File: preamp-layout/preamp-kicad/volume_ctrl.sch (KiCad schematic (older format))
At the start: 82 parts, among them J64 Conn_01x02_Male, J65 Conn_01x02_Male, J66 Conn_01x02_Male, J67 Conn_01x03_Female, J68 Conn_01x03_Female, J69 Conn_01x03_Male, J70 Conn_01x03_Male, J71 Conn_01x03_Male, U11 TL074CDR, U13 THAT2181, U14 THAT2181, U15 NJM2068M, U16 THAT2181, U17 THAT2181, U18 NJM2068M, U9 DAC5574

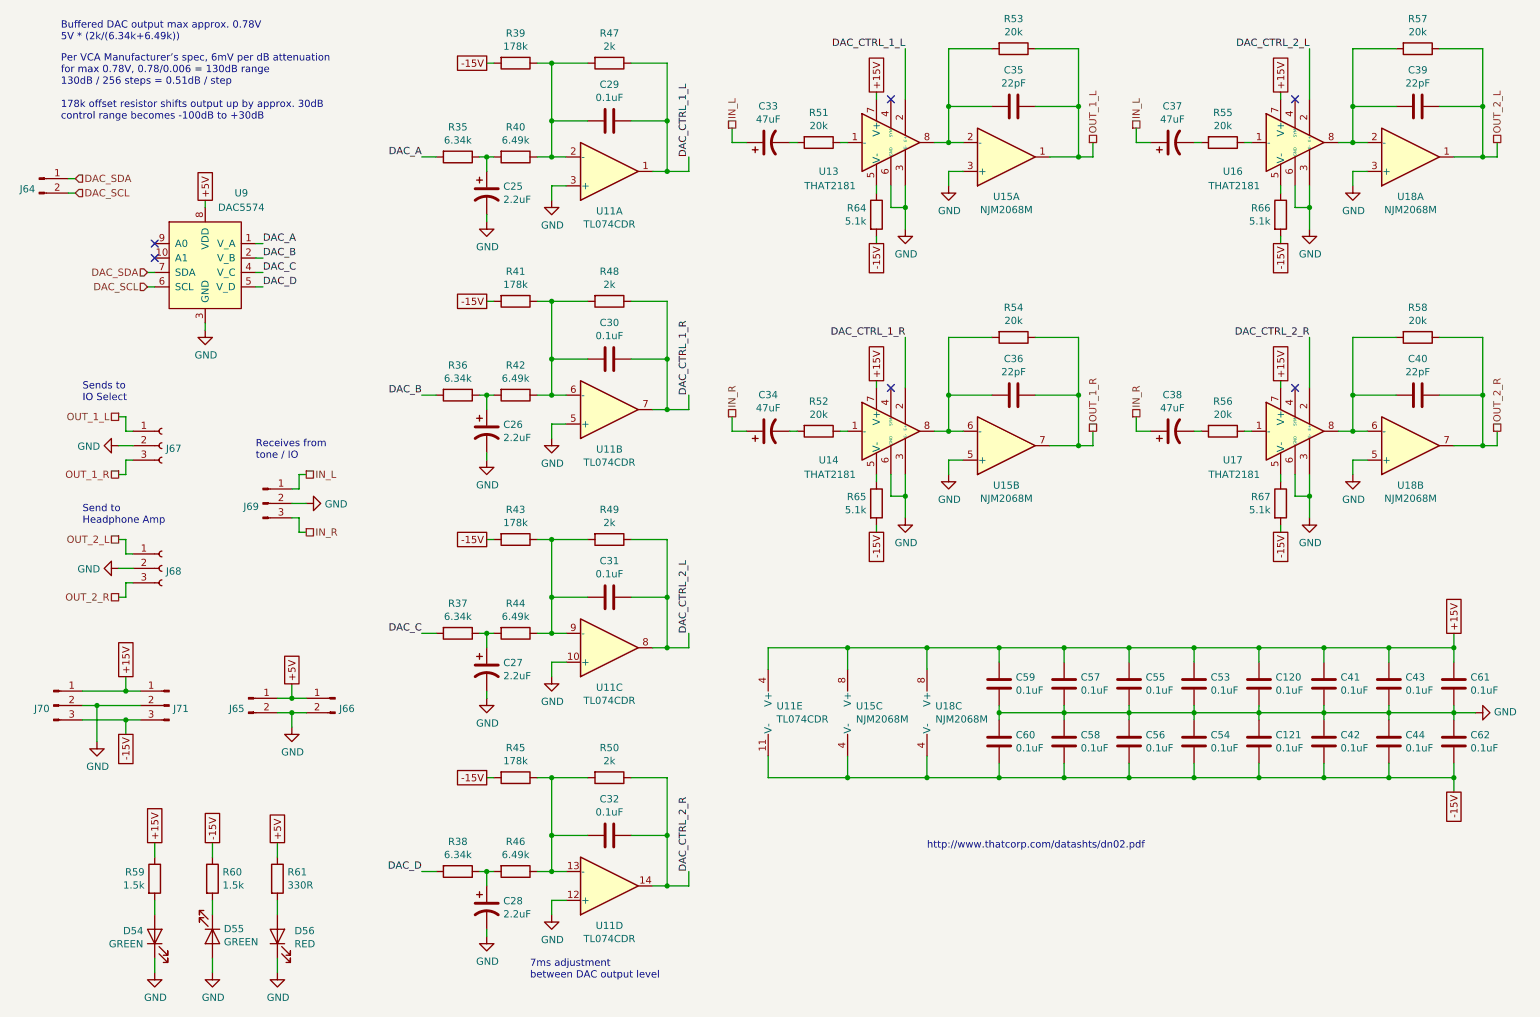
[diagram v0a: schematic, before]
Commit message: RefDes Update
Re-ran refdes assignment, updated BOM accordingly.
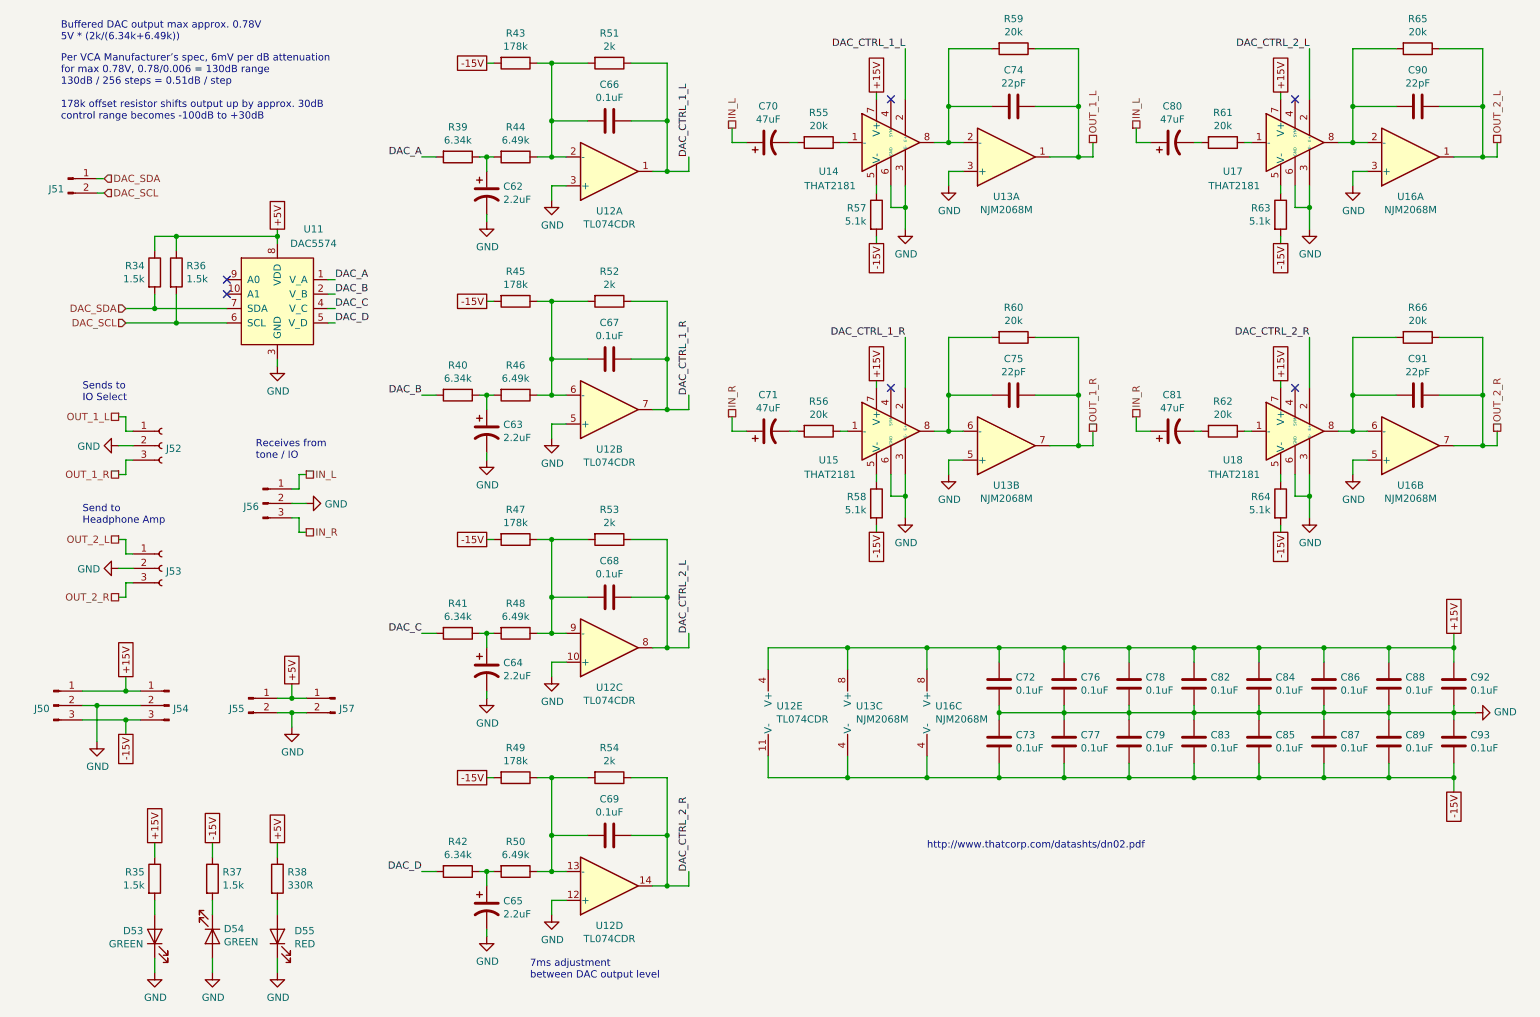
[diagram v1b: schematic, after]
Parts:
- added R34, R36: 1.5k, Resistor_SMD:R_1206_3216Metric_Pad1.42x1.75mm_HandSolder, symbol Device:R
- renumbered C25 to C62, C26 to C63, C27 to C64, C28 to C65, C29 to C66, C30 to C67, C31 to C68, C32 to C69, C33 to C70, C34 to C71, C59 to C72, C60 to C73, C35 to C74, C36 to C75, C57 to C76, C58 to C77, C55 to C78, C56 to C79, C37 to C80, C38 to C81, C53 to C82, C54 to C83, C120 to C84, C121 to C85, C41 to C86, C42 to C87, C43 to C88, C44 to C89, C39 to C90, C40 to C91, C61 to C92, C62 to C93, D54 to D53, D55 to D54, D56 to D55, J70 to J50, J64 to J51, J67 to J52, J68 to J53, J71 to J54, J65 to J55, J69 to J56, J66 to J57, R59 to R35, R60 to R37, R61 to R38, R35 to R39, R36 to R40, R37 to R41, R38 to R42, R39 to R43, R40 to R44, R41 to R45, R42 to R46, R43 to R47, R44 to R48, R45 to R49, R46 to R50, R47 to R51, R48 to R52, R49 to R53, R50 to R54, R51 to R55, R52 to R56, R64 to R57, R65 to R58, R53 to R59, R54 to R60, R55 to R61, R56 to R62, R66 to R63, R67 to R64, R57 to R65, R58 to R66, U9 to U11, U11 to U12, U15 to U13, U13 to U14, U14 to U15, U18 to U16, U16 to U17, U17 to U18
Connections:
- net +5V: now also R34.1, R36.1
- net DAC_SCL: now also R36.2
- net DAC_SDA: now also R34.2
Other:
- moved on the sheet: J51, U11

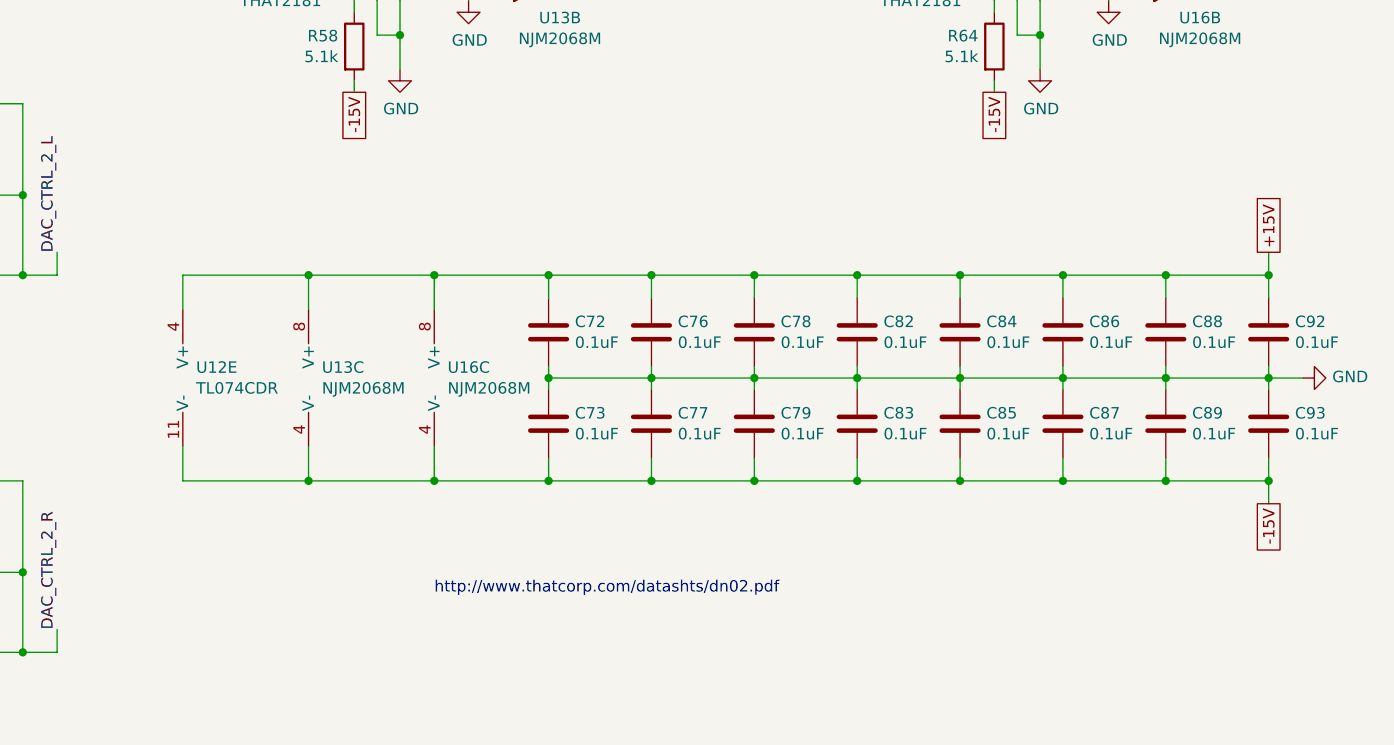
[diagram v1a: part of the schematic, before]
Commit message: Prelim PCB layout
Work done to lay out PCBs. Saving in anticipation of creating branch with a different input switching topology.
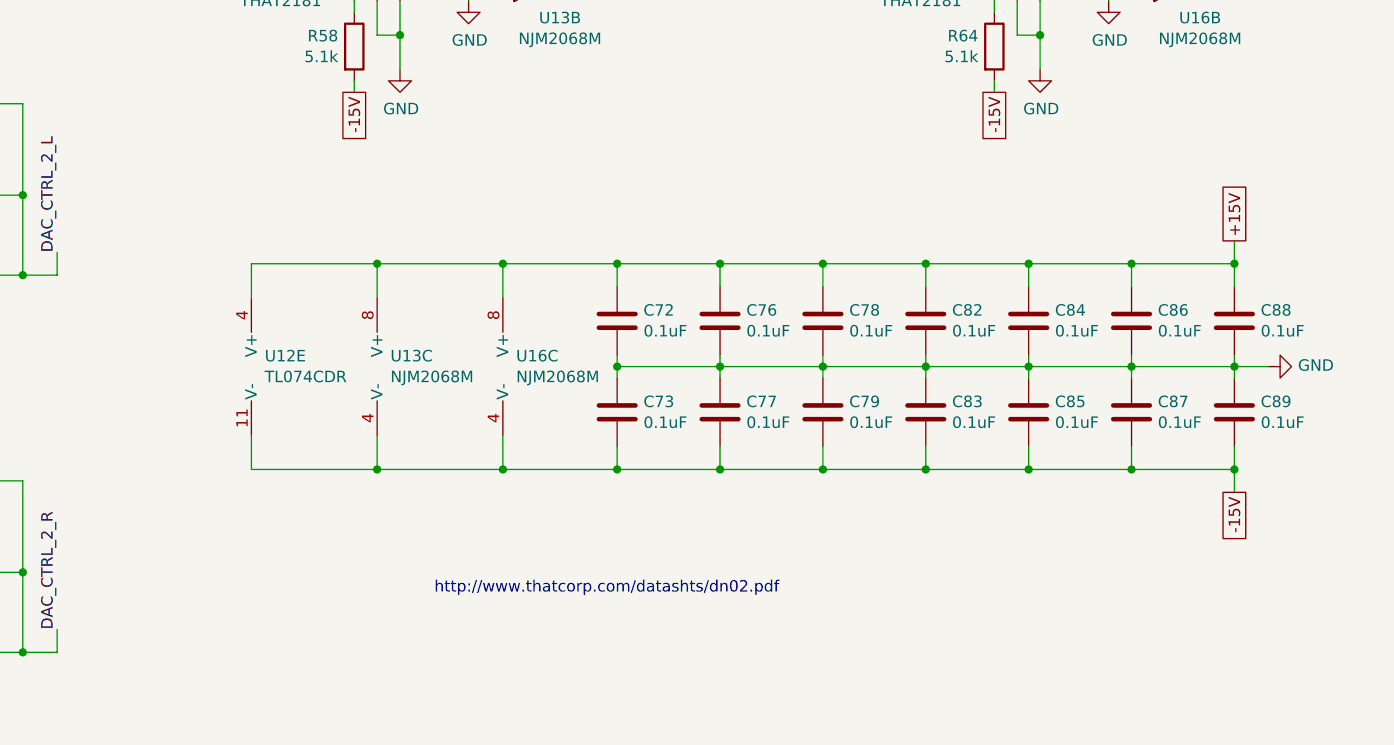
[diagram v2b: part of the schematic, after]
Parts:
- removed C92, C93: 0.1uF, Capacitor_SMD:C_0805_2012Metric_Pad1.15x1.40mm_HandSolder, symbol Device:C
- C62, C63, C64, C65: footprint (none) -> Capacitor_SMD:CP_Elec_4x5.4
- C70, C71, C80, C81: footprint (none) -> Capacitor_SMD:CP_Elec_6.3x5.4
- C74, C75, C90, C91: footprint (none) -> Capacitor_SMD:C_0805_2012Metric_Pad1.15x1.40mm_HandSolder
- R43: footprint Resistor_SMD:R_1206_3216Metric_Pad1.42x1.75mm_HandSolderv -> Resistor_SMD:R_1206_3216Metric_Pad1.42x1.75mm_HandSolder
- U11: footprint (none) -> Package_SO:MSOP-10-1EP_3x3mm_P0.5mm_EP1.68x1.88mm
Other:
- moved on the sheet: C72, C73, C76, C77, C78, C79, C82, C83, C84, C85, C86, C87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

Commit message: Periodic backup
Extensive changes as a result of PCB layout phase.
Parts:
- removed J52, J53: Conn_01x03_Female, Connector_PinHeader_2.54mm:PinHeader_1x03_P2.54mm_Vertical, symbol Connector:Conn_01x03_Female
- added J31: Conn_01x04_Male, Connector_PinHeader_2.54mm:PinHeader_1x04_P2.54mm_Vertical, symbol Connector:Conn_01x04_Male
- added J38: Conn_01x03_Male, Connector_JST:JST_EH_B3B-EH-A_1x03_P2.50mm_Vertical, symbol Connector:Conn_01x03_Male
- added J52: Conn_01x03_Male, Connector_PinHeader_2.54mm:PinHeader_1x03_P2.54mm_Vertical, symbol Connector:Conn_01x03_Male
- J50, J54: footprint Connector_JST:JST_EH_B3B-EH-A_1x03_P2.50mm_Vertical -> Connector_JST:JST_EH_S3B-EH_1x03_P2.50mm_Horizontal
- J51, J55, J57: footprint Connector_JST:JST_EH_B2B-EH-A_1x02_P2.50mm_Vertical -> Connector_JST:JST_EH_S2B-EH_1x02_P2.50mm_Horizontal
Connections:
- net +15V: now also J31.1 (Pin_1)
- net +5V: now also J31.3 (Pin_3)
- net -15V: now also J31.2 (Pin_2)
- net GND: now also J31.4 (Pin_4), J38.2 (Pin_2), J52.2 (Pin_2)
- net OUT_1_L: now also J52.1 (Pin_1)
- net OUT_1_R: now also J52.3 (Pin_3)
- net OUT_2_L: now also J38.1 (Pin_1)
- net OUT_2_R: now also J38.3 (Pin_3)
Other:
- moved on the sheet: D53, D54, D55, R35, R37, R38

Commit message: PCB layout
trying a different layout for the gain stage board, this serves as a reference point.
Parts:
- removed J31: Conn_01x04_Male, Connector_PinHeader_2.54mm:PinHeader_1x04_P2.54mm_Vertical, symbol Connector:Conn_01x04_Male
- C72, C73, C76, C77, C78, C79, C82, C83, C84, C85, C86, C87, C88, C89: footprint Capacitor_SMD:C_0805_2012Metric_Pad1.15x1.40mm_HandSolder -> Capacitor_SMD:C_1206_3216Metric_Pad1.42x1.75mm_HandSolder
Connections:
- net DAC_A: now also U11.2 (V_B); no longer U11.1 (V_A)
- net DAC_B: now also U11.1 (V_A); no longer U11.2 (V_B)
- net DAC_C: now also U11.5 (V_D); no longer U11.4 (V_C)
- net DAC_CTRL_1_L: now also U17.2 (E+); no longer U14.2 (E+)
- net DAC_CTRL_1_R: now also U18.2 (E+); no longer U15.2 (E+)
- net DAC_CTRL_2_L: now also U14.2 (E+); no longer U17.2 (E+)
- net DAC_CTRL_2_R: now also U15.2 (E+); no longer U18.2 (E+)
- net DAC_D: now also U11.4 (V_C); no longer U11.5 (V_D)
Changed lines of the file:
@@
 F 0 "C78" H 8815 5346 50  0000 L CNN
 F 1 "0.1uF" H 8815 5255 50  0000 L CNN
-F 2 "Capacitor_SMD:C_0805_2012Metric_Pad1.15x1.40mm_HandSolder" H 8738 5150 50  0001 C CNN
+F 2 "Capacitor_SMD:C_1206_3216Metric_Pad1.42x1.75mm_HandSolder" H 8738 5150 50  0001 C CNN
 F 3 "~" H 8700 5300 50  0001 C CNN
 	1    8700 5300
@@
 F 0 "C79" H 8815 5746 50  0000 L CNN
 F 1 "0.1uF" H 8815 5655 50  0000 L CNN
-F 2 "Capacitor_SMD:C_0805_2012Metric_Pad1.15x1.40mm_HandSolder" H 8738 5550 50  0001 C CNN
+F 2 "Capacitor_SMD:C_1206_3216Metric_Pad1.42x1.75mm_HandSolder" H 8738 5550 50  0001 C CNN
 F 3 "~" H 8700 5700 50  0001 C CNN
 	1    8700 5700
@@
 F 0 "C76" H 8365 5346 50  0000 L CNN
 F 1 "0.1uF" H 8365 5255 50  0000 L CNN
-F 2 "Capacitor_SMD:C_0805_2012Metric_Pad1.15x1.40mm_HandSolder" H 8288 5150 50  0001 C CNN
+F 2 "Capacitor_SMD:C_1206_3216Metric_Pad1.42x1.75mm_HandSolder" H 8288 5150 50  0001 C CNN
 F 3 "~" H 8250 5300 50  0001 C CNN
 	1    8250 5300
@@
 F 0 "C77" H 8365 5746 50  0000 L CNN
 F 1 "0.1uF" H 8365 5655 50  0000 L CNN
-F 2 "Capacitor_SMD:C_0805_2012Metric_Pad1.15x1.40mm_HandSolder" H 8288 5550 50  0001 C CNN
+F 2 "Capacitor_SMD:C_1206_3216Metric_Pad1.42x1.75mm_HandSolder" H 8288 5550 50  0001 C CNN
 F 3 "~" H 8250 5700 50  0001 C CNN
 	1    8250 5700
@@
 F 0 "C72" H 7915 5346 50  0000 L CNN
 F 1 "0.1uF" H 7915 5255 50  0000 L CNN
-F 2 "Capacitor_SMD:C_0805_2012Metric_Pad1.15x1.40mm_HandSolder" H 7838 5150 50  0001 C CNN
+F 2 "Capacitor_SMD:C_1206_3216Metric_Pad1.42x1.75mm_HandSolder" H 7838 5150 50  0001 C CNN
 F 3 "~" H 7800 5300 50  0001 C CNN
 	1    7800 5300
@@
 F 0 "C73" H 7915 5746 50  0000 L CNN
 F 1 "0.1uF" H 7915 5655 50  0000 L CNN
-F 2 "Capacitor_SMD:C_0805_2012Metric_Pad1.15x1.40mm_HandSolder" H 7838 5550 50  0001 C CNN
+F 2 "Capacitor_SMD:C_1206_3216Metric_Pad1.42x1.75mm_HandSolder" H 7838 5550 50  0001 C CNN
 F 3 "~" H 7800 5700 50  0001 C CNN
 	1    7800 5700
@@
 Wire Wire Line
 	6850 1300 6850 950
-Text Label 6850 950  2    50   ~ 0
+Text Label 9650 950  2    50   ~ 0
 DAC_CTRL_1_L
+Text Label 9650 2950 2    50   ~ 0
+DAC_CTRL_1_R
 Text Label 6850 2950 2    50   ~ 0
-DAC_CTRL_1_R
-Text Label 9650 950  2    50   ~ 0
-DAC_CTRL_2_L
-Text Label 9650 2950 2    50   ~ 0
 DAC_CTRL_2_R
 Wire Wire Line
@@
 F 0 "C82" H 9265 5346 50  0000 L CNN
 F 1 "0.1uF" H 9265 5255 50  0000 L CNN
-F 2 "Capacitor_SMD:C_0805_2012Metric_Pad1.15x1.40mm_HandSolder" H 9188 5150 50  0001 C CNN
+F 2 "Capacitor_SMD:C_1206_3216Metric_Pad1.42x1.75mm_HandSolder" H 9188 5150 50  0001 C CNN
 F 3 "~" H 9150 5300 50  0001 C CNN
 	1    9150 5300
@@
 F 0 "C83" H 9265 5746 50  0000 L CNN
 F 1 "0.1uF" H 9265 5655 50  0000 L CNN
-F 2 "Capacitor_SMD:C_0805_2012Metric_Pad1.15x1.40mm_HandSolder" H 9188 5550 50  0001 C CNN
+F 2 "Capacitor_SMD:C_1206_3216Metric_Pad1.42x1.75mm_HandSolder" H 9188 5550 50  0001 C CNN
 F 3 "~" H 9150 5700 50  0001 C CNN
 	1    9150 5700
@@
 F 0 "C88" H 10615 5346 50  0000 L CNN
 F 1 "0.1uF" H 10615 5255 50  0000 L CNN
-F 2 "Capacitor_SMD:C_0805_2012Metric_Pad1.15x1.40mm_HandSolder" H 10538 5150 50  0001 C CNN
+F 2 "Capacitor_SMD:C_1206_3216Metric_Pad1.42x1.75mm_HandSolder" H 10538 5150 50  0001 C CNN
 F 3 "~" H 10500 5300 50  0001 C CNN
 	1    10500 5300
@@
 F 0 "C89" H 10615 5746 50  0000 L CNN
 F 1 "0.1uF" H 10615 5655 50  0000 L CNN
-F 2 "Capacitor_SMD:C_0805_2012Metric_Pad1.15x1.40mm_HandSolder" H 10538 5550 50  0001 C CNN
+F 2 "Capacitor_SMD:C_1206_3216Metric_Pad1.42x1.75mm_HandSolder" H 10538 5550 50  0001 C CNN
 F 3 "~" H 10500 5700 50  0001 C CNN
 	1    10500 5700
@@
 F 0 "C86" H 10165 5346 50  0000 L CNN
 F 1 "0.1uF" H 10165 5255 50  0000 L CNN
-F 2 "Capacitor_SMD:C_0805_2012Metric_Pad1.15x1.40mm_HandSolder" H 10088 5150 50  0001 C CNN
+F 2 "Capacitor_SMD:C_1206_3216Metric_Pad1.42x1.75mm_HandSolder" H 10088 5150 50  0001 C CNN
 F 3 "~" H 10050 5300 50  0001 C CNN
 	1    10050 5300
@@
 F 0 "C87" H 10165 5746 50  0000 L CNN
 F 1 "0.1uF" H 10165 5655 50  0000 L CNN
-F 2 "Capacitor_SMD:C_0805_2012Metric_Pad1.15x1.40mm_HandSolder" H 10088 5550 50  0001 C CNN
+F 2 "Capacitor_SMD:C_1206_3216Metric_Pad1.42x1.75mm_HandSolder" H 10088 5550 50  0001 C CNN
 F 3 "~" H 10050 5700 50  0001 C CNN
 	1    10050 5700
@@
 Text HLabel 1450 2750 0    50   Input ~ 0
 DAC_SDA
+Text Label 2900 2650 0    50   ~ 0
+DAC_A
 Text Label 2900 2550 0    50   ~ 0
-DAC_A
-Text Label 2900 2650 0    50   ~ 0
 DAC_B
+Text Label 2900 2850 0    50   ~ 0
+DAC_C
 Text Label 2900 2750 0    50   ~ 0
-DAC_C
-Text Label 2900 2850 0    50   ~ 0
 DAC_D
 Wire Wire Line
@@
 F 0 "C84" H 9715 5346 50  0000 L CNN
 F 1 "0.1uF" H 9715 5255 50  0000 L CNN
-F 2 "Capacitor_SMD:C_0805_2012Metric_Pad1.15x1.40mm_HandSolder" H 9638 5150 50  0001 C CNN
+F 2 "Capacitor_SMD:C_1206_3216Metric_Pad1.42x1.75mm_HandSolder" H 9638 5150 50  0001 C CNN
 F 3 "~" H 9600 5300 50  0001 C CNN
 	1    9600 5300
@@
 F 0 "C85" H 9715 5746 50  0000 L CNN
 F 1 "0.1uF" H 9715 5655 50  0000 L CNN
-F 2 "Capacitor_SMD:C_0805_2012Metric_Pad1.15x1.40mm_HandSolder" H 9638 5550 50  0001 C CNN
+F 2 "Capacitor_SMD:C_1206_3216Metric_Pad1.42x1.75mm_HandSolder" H 9638 5550 50  0001 C CNN
 F 3 "~" H 9600 5700 50  0001 C CNN
 	1    9600 5700
@@
 	1    950  5500
 	1    0    0    -1
-$EndComp
-Wire Wire Line
-	1050 6700 1150 6700
-Text GLabel 1050 6700 0    50   UnSpc ~ 0
-+15V
-Text GLabel 1050 6800 0    50   UnSpc ~ 0
--15V
-Wire Wire Line
-	1050 6800 1150 6800
-Text GLabel 1050 6900 0    50   UnSpc ~ 0
-+5V
-Wire Wire Line
-	1050 6900 1150 6900
-Wire Wire Line
-	1150 7000 1150 7100
-$Comp
-L power:GND #PWR044
-U 1 1 5F0E70B1
-P 1150 7100
-AR Path="/6009D432/5F0E70B1" Ref="#PWR044"  Part="1"
-AR Path="/5E2D8DA2/5F0E70B1" Ref="#PWR?"  Part="1"
-F 0 "#PWR044" H 1150 6850 50  0001 C CNN
-F 1 "GND" H 1155 6927 50  0000 C CNN
-F 2 "" H 1150 7100 50  0001 C CNN
-F 3 "" H 1150 7100 50  0001 C CNN
-	1    1150 7100
-	1    0    0    -1
-$EndComp
-$Comp
-L Connector:Conn_01x04_Male J31
-U 1 1 5F109FB1
-P 1350 6800
-F 0 "J31" H 1322 6728 50  0000 R CNN
-F 1 "Conn_01x04_Male" H 1322 6683 50  0001 R CNN
-F 2 "Connector_PinHeader_2.54mm:PinHeader_1x04_P2.54mm_Vertical" H 1350 6800 50  0001 C CNN
-F 3 "~" H 1350 6800 50  0001 C CNN
-	1    1350 6800
-	-1   0    0    -1
 $EndComp
 $Comp
@@
 	-1   0    0    -1
 $EndComp
+Text Label 6850 950  2    50   ~ 0
+DAC_CTRL_2_L
 $EndSCHEMATC
